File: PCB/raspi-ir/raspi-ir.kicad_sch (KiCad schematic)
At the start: 32 parts, among them J1 Conn_01x03_Pin, J2 HR3P-N4EC-00000, J3 Conn_02x20_Odd_Even, J4 HR3P-N4EC-00000, J5 HR3P-N4EC-00000, J6 HR3P-N4EC-00000, Q1 MMBT2222A, Q2 MMBT2222A, Q3 MMBT2222A, Q4 MMBT2222A, U1 TSOP38238, U2 PCF8523T, Y1 Crystal

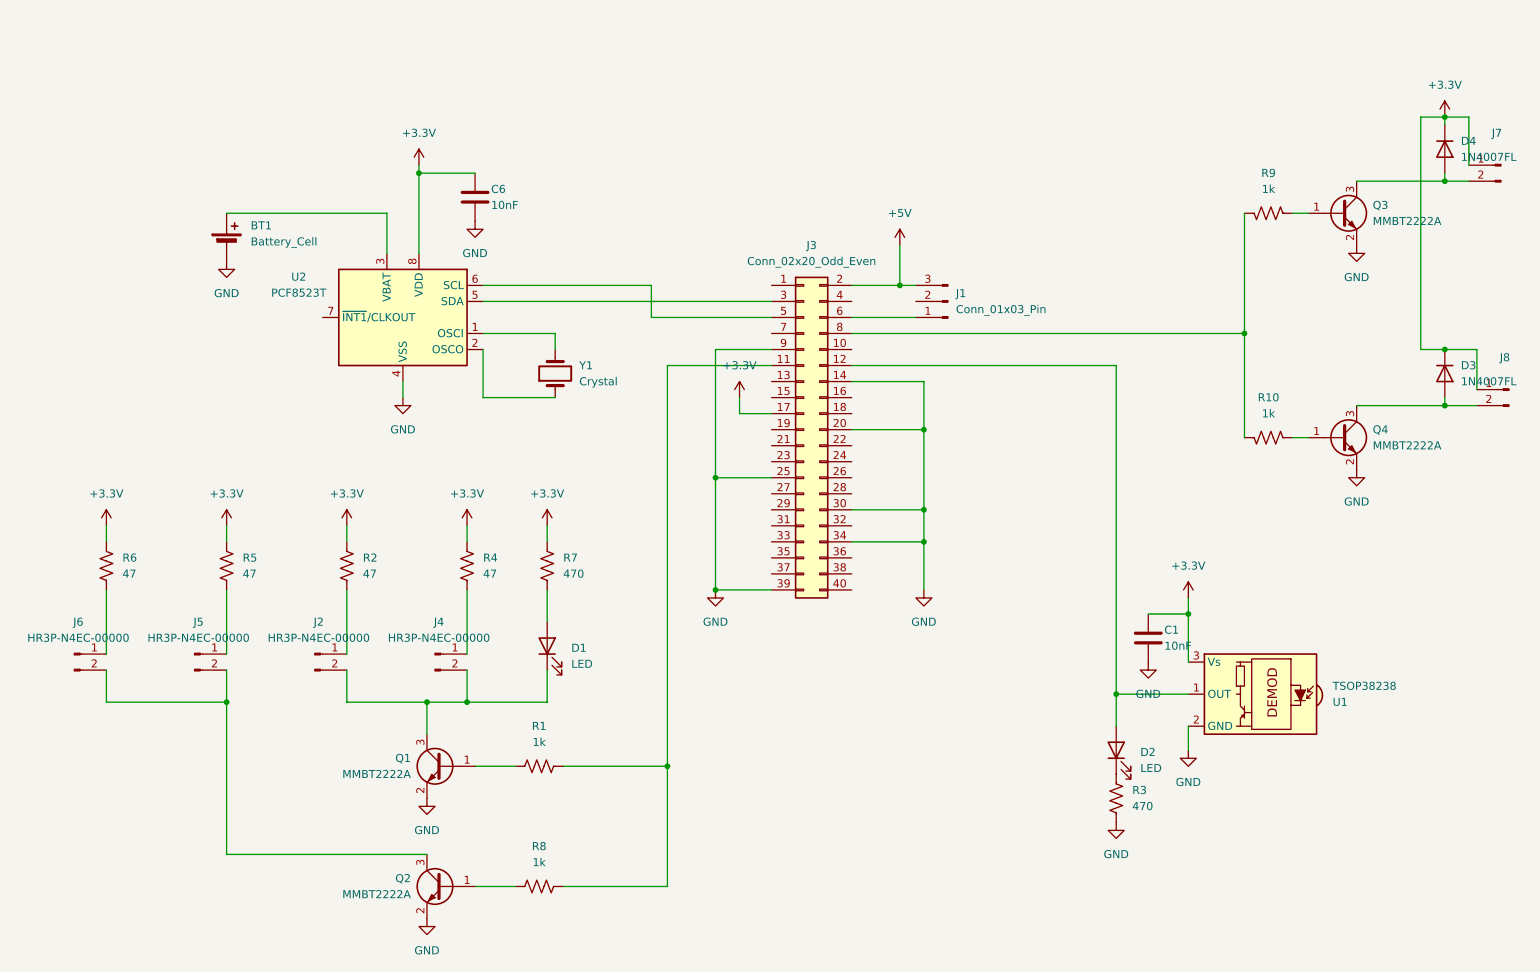
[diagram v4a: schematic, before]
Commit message: PCB redesigned to version 2
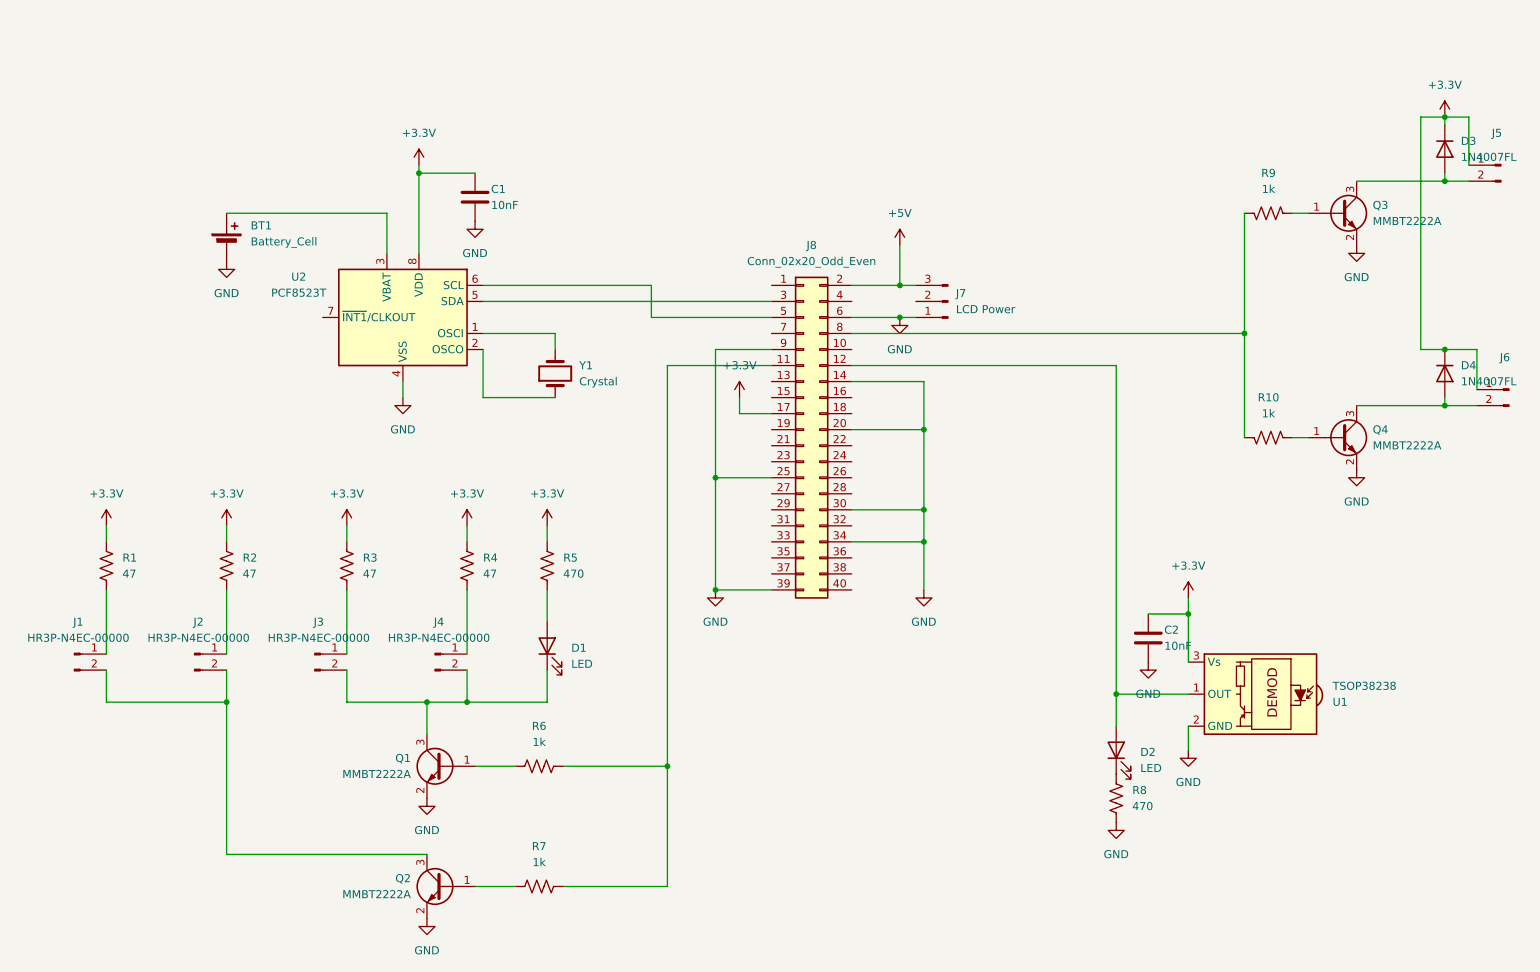
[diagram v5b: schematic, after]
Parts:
- J7: renamed from J1; value Conn_01x03_Pin -> LCD Power
- renumbered C6 to C1, C1 to C2, D4 to D3, D3 to D4, J6 to J1, J5 to J2, J2 to J3, J7 to J5, J8 to J6, J3 to J8, R6 to R1, R5 to R2, R2 to R3, R7 to R5, R1 to R6, R8 to R7, R3 to R8
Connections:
- net GND: now also J7.1 (Pin_1), J8.6 (Pin_6)
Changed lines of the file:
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@@
 	)
 	(junction
+		(at 161.29 63.5)
+		(diameter 0)
+		(color 0 0 0 0)
+	)
+	(junction
 		(at 165.1 93.98)
 		(diameter 0)
@@
 	(wire
 		(pts
+			(xy 161.29 63.5) (xy 163.83 63.5)
+		)
+		(stroke
+			(width 0)
+			(type default)
+		)
+	)
+	(wire
+		(pts
 			(xy 85.09 39.37) (xy 85.09 40.64)
 		)
@@
 	(wire
 		(pts
-			(xy 153.67 63.5) (xy 163.83 63.5)
+			(xy 153.67 63.5) (xy 161.29 63.5)
 		)
 		(stroke
@@
 		(dnp no)
 		(fields_autoplaced yes)
-		(property "Reference" "R5"
+		(property "Reference" "R2"
 			(at 57.15 101.5999 0)
 			(effects
@@
 			(project "raspi-ir"
 				(path "/44299703-577c-4e07-82b2-1ac696b0eb61"
-					(reference "R5")
+					(reference "R2")
+					(unit 1)
+				)
+			)
+		)
+	)
+	(symbol
+		(lib_id "power:GND")
+		(at 161.29 63.5 0)
+		(unit 1)
+		(exclude_from_sim no)
+		(in_bom yes)
+		(on_board yes)
+		(dnp no)
+		(fields_autoplaced yes)
+		(property "Reference" "#PWR020"
+			(at 161.29 69.85 0)
+			(effects
+				(font
+					(size 1.27 1.27)
+				)
+				(hide yes)
+			)
+		)
+		(property "Value" "GND"
+			(at 161.29 68.58 0)
+			(effects
+				(font
+					(size 1.27 1.27)
+				)
+			)
+		)
+		(property "Footprint" ""
+			(at 161.29 63.5 0)
+			(effects
+				(font
+					(size 1.27 1.27)
+				)
+				(hide yes)
+			)
+		)
+		(property "Datasheet" ""
+			(at 161.29 63.5 0)
+			(effects
+				(font
+					(size 1.27 1.27)
+				)
+				(hide yes)
+			)
+		)
+		(property "Description" "Power symbol creates a global label with name \"GND\" , ground"
+			(at 161.29 63.5 0)
+			(effects
+				(font
+					(size 1.27 1.27)
+				)
+				(hide yes)
+			)
+		)
+		(pin "1"
+		)
+		(instances
+			(project "raspi-ir"
+				(path "/44299703-577c-4e07-82b2-1ac696b0eb61"
+					(reference "#PWR020")
 					(unit 1)
 				)
@@
 		(on_board yes)
 		(dnp no)
-		(property "Reference" "C6"
+		(property "Reference" "C1"
 			(at 96.52 43.18 0)
 			(effects
@@
 			(project "raspi-ir"
 				(path "/44299703-577c-4e07-82b2-1ac696b0eb61"
-					(reference "C6")
+					(reference "C1")
 					(unit 1)
 				)
@@
 		(dnp no)
 		(fields_autoplaced yes)
-		(property "Reference" "R3"
+		(property "Reference" "R8"
 			(at 198.12 138.4299 0)
 			(effects
@@
 			(project "raspi-ir"
 				(path "/44299703-577c-4e07-82b2-1ac696b0eb61"
-					(reference "R3")
+					(reference "R8")
 					(unit 1)
 				)
@@
 		(dnp no)
 		(fields_autoplaced yes)
-		(property "Reference" "R6"
+		(property "Reference" "R1"
 			(at 38.1 101.5999 0)
 			(effects
@@
 			(project "raspi-ir"
 				(path "/44299703-577c-4e07-82b2-1ac696b0eb61"
-					(reference "R6")
+					(reference "R1")
 					(unit 1)
 				)
@@
 		(dnp no)
 		(fields_autoplaced yes)
-		(property "Reference" "J6"
+		(property "Reference" "J1"
 			(at 31.115 111.76 0)
 			(effects
@@
 			(project "raspi-ir"
 				(path "/44299703-577c-4e07-82b2-1ac696b0eb61"
-					(reference "J6")
+					(reference "J1")
 					(unit 1)
 				)
@@
 		(dnp no)
 		(fields_autoplaced yes)
-		(property "Reference" "D4"
+		(property "Reference" "D3"
 			(at 250.19 35.5599 90)
 			(effects
@@
 			(project "raspi-ir"
 				(path "/44299703-577c-4e07-82b2-1ac696b0eb61"
-					(reference "D4")
+					(reference "D3")
 					(unit 1)
 				)
@@
 		(dnp no)
 		(fields_autoplaced yes)
-		(property "Reference" "R7"
+		(property "Reference" "R5"
 			(at 107.95 101.5999 0)
 			(effects
@@
 			(project "raspi-ir"
 				(path "/44299703-577c-4e07-82b2-1ac696b0eb61"
-					(reference "R7")
+					(reference "R5")
 					(unit 1)
 				)
@@
 		(dnp no)
 		(fields_autoplaced yes)
-		(property "Reference" "R2"
+		(property "Reference" "R3"
 			(at 76.2 101.5999 0)
 			(effects
@@
 			(project "raspi-ir"
 				(path "/44299703-577c-4e07-82b2-1ac696b0eb61"
-					(reference "R2")
+					(reference "R3")
 					(unit 1)
 				)
@@
 		(dnp no)
 		(fields_autoplaced yes)
-		(property "Reference" "D3"
+		(property "Reference" "D4"
 			(at 250.19 71.1199 90)
 			(effects
@@
 			(project "raspi-ir"
 				(path "/44299703-577c-4e07-82b2-1ac696b0eb61"
-					(reference "D3")
+					(reference "D4")
 					(unit 1)
 				)
@@
 		(dnp no)
 		(fields_autoplaced yes)
-		(property "Reference" "R8"
+		(property "Reference" "R7"
 			(at 104.14 147.32 90)
 			(effects
@@
 			(project "raspi-ir"
 				(path "/44299703-577c-4e07-82b2-1ac696b0eb61"
-					(reference "R8")
+					(reference "R7")
 					(unit 1)
 				)
@@
 		(dnp no)
 		(fields_autoplaced yes)
-		(property "Reference" "J1"
+		(property "Reference" "J7"
 			(at 170.18 59.6899 0)
 			(effects
@@
 			)
 		)
-		(property "Value" "Conn_01x03_Pin"
+		(property "Value" "LCD Power"
 			(at 170.18 62.2299 0)
 			(effects
@@
 			(project ""
 				(path "/44299703-577c-4e07-82b2-1ac696b0eb61"
-					(reference "J1")
+					(reference "J7")
 					(unit 1)
 				)
@@
 		(dnp no)
 		(fields_autoplaced yes)
-		(property "Reference" "J3"
+		(property "Reference" "J8"
 			(at 147.32 52.07 0)
 			(effects
@@
 			(project ""
 				(path "/44299703-577c-4e07-82b2-1ac696b0eb61"
-					(reference "J3")
+					(reference "J8")
 					(unit 1)
 				)
@@
 		(on_board yes)
 		(dnp no)
-		(property "Reference" "J8"
+		(property "Reference" "J6"
 			(at 257.175 69.85 0)
 			(effects
@@
 			(project "raspi-ir"
 				(path "/44299703-577c-4e07-82b2-1ac696b0eb61"
-					(reference "J8")
+					(reference "J6")
 					(unit 1)
 				)
@@
 		(dnp no)
 		(fields_autoplaced yes)
-		(property "Reference" "R1"
+		(property "Reference" "R6"
 			(at 104.14 128.27 90)
 			(effects
@@
 			(project ""
 				(path "/44299703-577c-4e07-82b2-1ac696b0eb61"
-					(reference "R1")
+					(reference "R6")
 					(unit 1)
 				)
@@
 		(on_board yes)
 		(dnp no)
-		(property "Reference" "J7"
+		(property "Reference" "J5"
 			(at 255.905 34.29 0)
 			(effects
@@
 			(project "raspi-ir"
 				(path "/44299703-577c-4e07-82b2-1ac696b0eb61"
-					(reference "J7")
+					(reference "J5")
 					(unit 1)
 				)
@@
 		(on_board yes)
 		(dnp no)
-		(property "Reference" "C1"
+		(property "Reference" "C2"
 			(at 203.2 113.03 0)
 			(effects
@@
 			(project "raspi-ir"
 				(path "/44299703-577c-4e07-82b2-1ac696b0eb61"
-					(reference "C1")
+					(reference "C2")
 					(unit 1)
 				)
@@
 		(dnp no)
 		(fields_autoplaced yes)
-		(property "Reference" "J5"
+		(property "Reference" "J2"
 			(at 50.165 111.76 0)
 			(effects
@@
 			(project "raspi-ir"
 				(path "/44299703-577c-4e07-82b2-1ac696b0eb61"
-					(reference "J5")
+					(reference "J2")
 					(unit 1)
 				)
@@
 		(dnp no)
 		(fields_autoplaced yes)
-		(property "Reference" "J2"
+		(property "Reference" "J3"
 			(at 69.215 111.76 0)
 			(effects
@@
 			(project ""
 				(path "/44299703-577c-4e07-82b2-1ac696b0eb61"
-					(reference "J2")
+					(reference "J3")
 					(unit 1)
 				)
